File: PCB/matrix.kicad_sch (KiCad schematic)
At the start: 204 parts

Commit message: LED Diode Placement finished
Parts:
- renumbered D66 to D65, D67 to D66, D68 to D67, D69 to D68, D70 to D69, D71 to D70, D72 to D71, D73 to D72, D74 to D73, D75 to D74, D76 to D75, D77 to D76, D78 to D77, D79 to D78, D80 to D79, D81 to D80, D82 to D81, D83 to D82, D65 to D83, D87 to D84, D88 to D85, D89 to D86, D90 to D87, D91 to D88, D92 to D89, D93 to D90, D94 to D91, D95 to D92, D96 to D93, D97 to D94, D98 to D95, D84 to D96, D85 to D97, D86 to D98, MX66 to MX65, MX67 to MX66, MX68 to MX67, MX69 to MX68, MX70 to MX69, MX71 to MX70, MX72 to MX71, MX73 to MX72, MX74 to MX73, MX75 to MX74, MX76 to MX75, MX77 to MX76, MX78 to MX77, MX79 to MX78, MX80 to MX79, MX81 to MX80, MX82 to MX81, MX83 to MX82, MX65 to MX83, MX87 to MX84, MX88 to MX85, MX89 to MX86, MX90 to MX87, MX91 to MX88, MX92 to MX89, MX93 to MX90, MX94 to MX91, MX95 to MX92, MX96 to MX93, MX97 to MX94, MX98 to MX95, MX84 to MX96, MX85 to MX97, MX86 to MX98

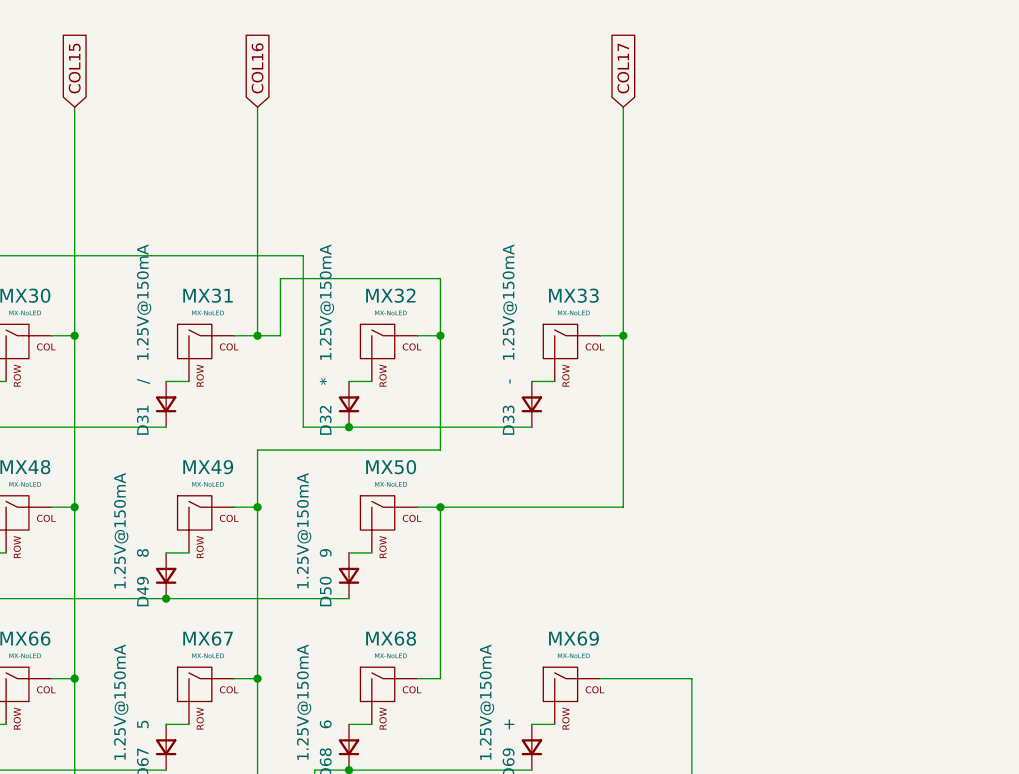
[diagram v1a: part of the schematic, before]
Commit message: LED +5 Wired, COL and ROW Buses nearly finished
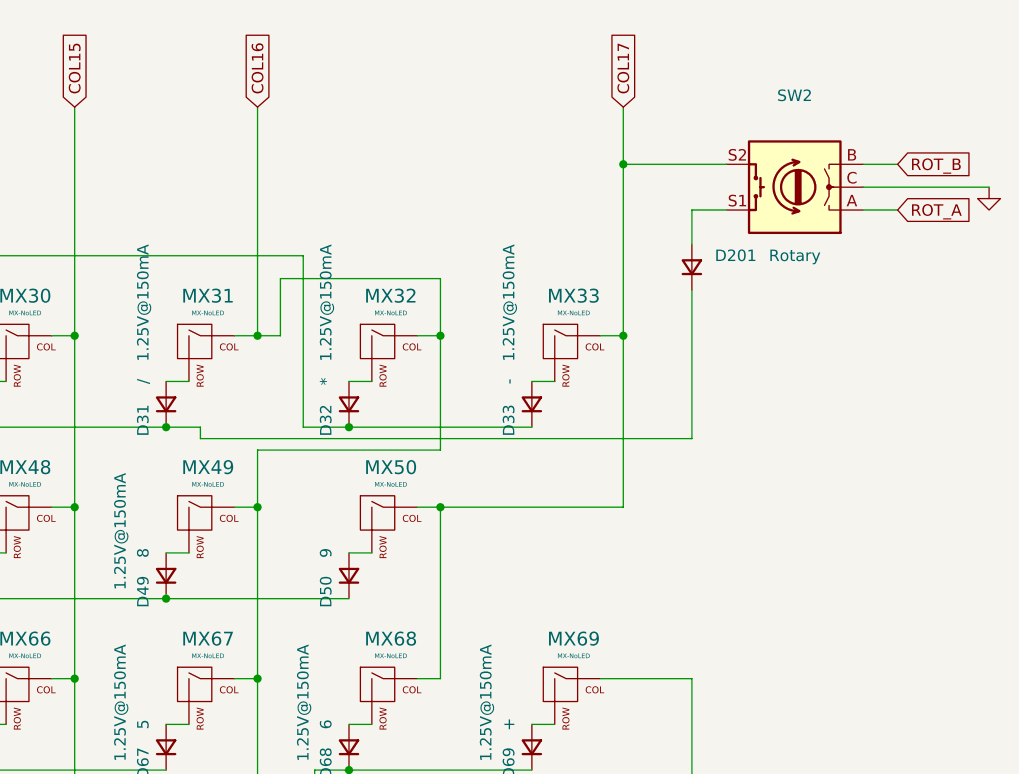
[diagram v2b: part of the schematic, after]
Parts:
- added D201: (no value), symbol led:D_Small
- added SW2: (no value), symbol Device:RotaryEncoder_Switch
- D50: value 1.25V@150mA -> (none); footprint led:D_SOD-123 -> (none)
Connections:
- net COL17: now also SW2.S2
- net ROW1: now also D201.1 (K)
- new net: D201.2 (A), SW2.S1
- new net GND: SW2.C
- new net ROT_A: SW2.A
- new net ROT_B: SW2.B
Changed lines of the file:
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@@
   (junction (at 322.58 158.75) (diameter 0) (color 0 0 0 0)
   )
+  (junction (at 459.74 168.91) (diameter 0) (color 0 0 0 0)
+  )
   (junction (at 322.58 196.85) (diameter 0) (color 0 0 0 0)
   )
@@
   (junction (at 416.56 215.9) (diameter 0) (color 0 0 0 0)
   )
+  (junction (at 510.54 139.7) (diameter 0) (color 0 0 0 0)
+  )
   (junction (at 302.26 158.75) (diameter 0) (color 0 0 0 0)
   )
@@
     (stroke (width 0) (type default) (color 0 0 0 0))
   )
+  (wire (pts (xy 510.54 139.7) (xy 521.97 139.7))
+    (stroke (width 0) (type default) (color 0 0 0 0))
+  )
   (wire (pts (xy 170.18 182.88) (xy 172.72 182.88))
     (stroke (width 0) (type default) (color 0 0 0 0))
@@
     (stroke (width 0) (type default) (color 0 0 0 0))
   )
+  (wire (pts (xy 537.21 144.78) (xy 541.02 144.78))
+    (stroke (width 0) (type default) (color 0 0 0 0))
+  )
   (wire (pts (xy 312.42 144.78) (xy 314.96 144.78))
     (stroke (width 0) (type default) (color 0 0 0 0))
@@
     (stroke (width 0) (type default) (color 0 0 0 0))
   )
+  (wire (pts (xy 537.21 142.24) (xy 551.18 142.24))
+    (stroke (width 0) (type default) (color 0 0 0 0))
+  )
   (wire (pts (xy 439.42 163.83) (xy 441.96 163.83))
     (stroke (width 0) (type default) (color 0 0 0 0))
@@
     (stroke (width 0) (type default) (color 0 0 0 0))
   )
+  (wire (pts (xy 537.21 139.7) (xy 541.02 139.7))
+    (stroke (width 0) (type default) (color 0 0 0 0))
+  )
   (wire (pts (xy 469.9 234.95) (xy 467.36 234.95))
     (stroke (width 0) (type default) (color 0 0 0 0))
@@
     (stroke (width 0) (type default) (color 0 0 0 0))
   )
+  (wire (pts (xy 510.54 139.7) (xy 510.54 133.35))
+    (stroke (width 0) (type default) (color 0 0 0 0))
+  )
   (wire (pts (xy 302.26 158.75) (xy 299.72 158.75))
     (stroke (width 0) (type default) (color 0 0 0 0))
@@
     (stroke (width 0) (type default) (color 0 0 0 0))
   )
+  (wire (pts (xy 518.16 153.67) (xy 518.16 170.18))
+    (stroke (width 0) (type default) (color 0 0 0 0))
+  )
   (wire (pts (xy 271.78 168.91) (xy 292.1 168.91))
     (stroke (width 0) (type default) (color 0 0 0 0))
@@
     (stroke (width 0) (type default) (color 0 0 0 0))
   )
+  (wire (pts (xy 463.55 170.18) (xy 518.16 170.18))
+    (stroke (width 0) (type default) (color 0 0 0 0))
+  )
   (wire (pts (xy 231.14 220.98) (xy 233.68 220.98))
     (stroke (width 0) (type default) (color 0 0 0 0))
@@
     (stroke (width 0) (type default) (color 0 0 0 0))
   )
+  (wire (pts (xy 463.55 168.91) (xy 463.55 170.18))
+    (stroke (width 0) (type default) (color 0 0 0 0))
+  )
   (wire (pts (xy 220.98 196.85) (xy 220.98 215.9))
     (stroke (width 0) (type default) (color 0 0 0 0))
@@
     (stroke (width 0) (type default) (color 0 0 0 0))
   )
+  (wire (pts (xy 459.74 168.91) (xy 463.55 168.91))
+    (stroke (width 0) (type default) (color 0 0 0 0))
+  )
   (wire (pts (xy 406.4 187.96) (xy 439.42 187.96))
     (stroke (width 0) (type default) (color 0 0 0 0))
@@
     (stroke (width 0) (type default) (color 0 0 0 0))
   )
-  (wire (pts (xy 510.54 158.75) (xy 510.54 133.35))
+  (wire (pts (xy 510.54 158.75) (xy 510.54 139.7))
     (stroke (width 0) (type default) (color 0 0 0 0))
   )
@@
     (stroke (width 0) (type default) (color 0 0 0 0))
   )
+  (wire (pts (xy 518.16 144.78) (xy 518.16 148.59))
+    (stroke (width 0) (type default) (color 0 0 0 0))
+  )
+  (wire (pts (xy 521.97 144.78) (xy 518.16 144.78))
+    (stroke (width 0) (type default) (color 0 0 0 0))
+  )
   (wire (pts (xy 116.84 196.85) (xy 119.38 196.85))
     (stroke (width 0) (type default) (color 0 0 0 0))
@@
     )
   )
+  (global_label "ROT_A" (shape input) (at 541.02 144.78 0) (fields_autoplaced)
+    (effects (font (size 1.27 1.27)) (justify left))
+    (property "Intersheet References" "${INTERSHEET_REFS}" (id 0) (at 548.9685 144.7006 0)
+      (effects (font (size 1.27 1.27)) (justify left) hide)
+    )
+  )
   (global_label "COL12" (shape input) (at 342.9 133.35 90) (fields_autoplaced)
     (effects (font (size 1.27 1.27)) (justify left))
@@
     )
   )
+  (global_label "ROT_B" (shape input) (at 541.02 139.7 0) (fields_autoplaced)
+    (effects (font (size 1.27 1.27)) (justify left))
+    (property "Intersheet References" "${INTERSHEET_REFS}" (id 0) (at 549.1499 139.6206 0)
+      (effects (font (size 1.27 1.27)) (justify left) hide)
+    )
+  )
   (global_label "COL1" (shape input) (at 119.38 133.35 90) (fields_autoplaced)
     (effects (font (size 1.27 1.27)) (justify left))
@@
       (effects (font (size 1.27 1.27)) (justify right))
     )
-    (property "Value" "1.25V@150mA" (id 1) (at 474.98 173.99 0)
+    (property "Value" "" (id 1) (at 474.98 173.99 0)
       (effects (font (size 1.27 1.27)) (justify right))
     )
-    (property "Footprint" "led:D_SOD-123" (id 2) (at 480.06 185.42 90)
+    (property "Footprint" "" (id 2) (at 480.06 185.42 90)
       (effects (font (size 1.27 1.27)) hide)
     )
@@
     (pin "2")
   )
+  (symbol (lib_id "power:GND") (at 551.18 142.24 0) (unit 1)
+    (in_bom yes) (on_board yes) (fields_autoplaced)
+    (property "Reference" "#PWR0216" (id 0) (at 551.18 148.59 0)
+      (effects (font (size 1.27 1.27)) hide)
+    )
+    (property "Value" "" (id 1) (at 551.18 147.32 0))
+    (property "Footprint" "" (id 2) (at 551.18 142.24 0)
+      (effects (font (size 1.27 1.27)) hide)
+    )
+    (property "Datasheet" "" (id 3) (at 551.18 142.24 0)
+      (effects (font (size 1.27 1.27)) hide)
+    )
+    (pin "1")
+  )
   (symbol (lib_id "Device:D_Small") (at 170.18 166.37 90) (unit 1)
     (in_bom yes) (on_board yes)
@@
     (pin "2")
   )
+  (symbol (lib_id "Device:RotaryEncoder_Switch") (at 529.59 142.24 180) (unit 1)
+    (in_bom yes) (on_board yes) (fields_autoplaced)
+    (property "Reference" "SW2" (id 0) (at 529.59 132.08 0))
+    (property "Value" "" (id 1) (at 529.59 134.62 0))
+    (property "Footprint" "" (id 2) (at 533.4 146.304 0)
+      (effects (font (size 1.27 1.27)) hide)
+    )
+    (property "Datasheet" "~" (id 3) (at 529.59 148.844 0)
+      (effects (font (size 1.27 1.27)) hide)
+    )
+    (pin "A")
+    (pin "B")
+    (pin "C")
+    (pin "S1")
+    (pin "S2")
+  )
   (symbol (lib_id "pcb-rescue:MX-NoLED-MX_Alps_Hybrid") (at 153.67 160.02 0) (unit 1)
     (in_bom yes) (on_board yes)
@@
     (pin "1")
     (pin "2")
+  )
+  (symbol (lib_id "led:D_Small") (at 518.16 151.13 90) (unit 1)
+    (in_bom yes) (on_board yes)
+    (property "Reference" "D201" (id 0) (at 520.7 149.8599 90)
+      (effects (font (size 1.27 1.27)) (justify right))
+    )
+    (property "Value" "" (id 1) (at 520.7 152.3999 90)
+      (effects (font (size 1.27 1.27)) (justify right))
+    )
+    (property "Footprint" "" (id 2) (at 518.16 140.97 90)
+      (effects (font (size 1.27 1.27)) hide)
+    )
+    (property "Datasheet" "~" (id 3) (at 518.16 151.13 90)
+      (effects (font (size 1.27 1.27)) hide)
+    )
+    (property "Name" "Rotary" (id 4) (at 529.59 149.86 90))
+    (pin "1")
+    (pin "2")

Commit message: Fixed all Errors
Only 1009 Warnings remain :D
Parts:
- removed MX101: MX-NoLED, kailh-switches-hotswap:Kailh-Hotswap-6.25U, symbol pcb-rescue:MX-NoLED-MX_Alps_Hybrid
- removed MX102: MX-NoLED, kailh-switches-hotswap:Kailh-Hotswap-7U, symbol pcb-rescue:MX-NoLED-MX_Alps_Hybrid
- removed MX103: MX-NoLED, kailh-switches-hotswap:Kailh-Hotswap-1U, symbol pcb-rescue:MX-NoLED-MX_Alps_Hybrid
- removed MX104: MX-NoLED, kailh-switches-hotswap:Kailh-Hotswap-1.25U, symbol pcb-rescue:MX-NoLED-MX_Alps_Hybrid
- D201, D50: value (none) -> 1.25V@150mA; footprint (none) -> led:D_SOD-123
- MX1, MX10, MX100, MX11, MX12, MX13, MX14, MX15, MX16, MX17, MX18, MX19, MX2, MX20, MX21, MX22, MX23, MX24, MX25, MX26, MX27, MX29, MX3, MX30, MX31, MX32, MX33, MX35, MX36, MX37, MX38, MX39, MX4, MX40, MX41, MX42, MX43, MX44, MX45, MX46, MX47, MX48, MX49, MX5, MX50, MX52, MX53, MX54, MX55, MX56, MX57, MX58, MX59, MX6, MX60, MX61, MX62, MX63, MX65, MX66, MX67, MX68, MX7, MX71, MX72, MX73, MX74, MX75, MX76, MX77, MX78, MX79, MX8, MX80, MX81, MX83, MX84, MX85, MX86, MX87, MX9, MX90, MX94, MX95, MX96, MX97, MX98: footprint kailh-switches-hotswap:Kailh-Hotswap-1U -> (none)
- MX28, MX99: footprint kailh-switches-hotswap:Kailh-Hotswap-2U -> (none)
- MX34, MX89: footprint kailh-switches-hotswap:Kailh-Hotswap-1.5U -> (none)
- MX51, MX82: footprint kailh-switches-hotswap:Kailh-Hotswap-1.75U -> (none)
- MX64: footprint kailh-switches-hotswap:Kailh-Hotswap-EnterISO -> (none)
- MX69, MX88: footprint kailh-switches-hotswap:Kailh-Hotswap-2U-Vertical -> (none)
- MX70, MX91, MX93: footprint kailh-switches-hotswap:Kailh-Hotswap-1.25U -> (none)
- MX92: footprint kailh-switches-hotswap:Kailh-Hotswap-6U -> (none)
- SW2: value (none) -> RotaryEncoder_Switch; footprint (none) -> led:RotaryEncoder_EC11E-Switch

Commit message: 3D Models
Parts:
- D1, D10, D100, D11, D12, D13, D14, D15, D16, D17, D18, D19, D2, D20, D201, D21, D22, D23, D24, D25, D26, D27, D28, D29, D3, D30, D31, D32, D33, D34, D35, D36, D37, D38, D39, D4, D40, D41, D42, D43, D44, D45, D46, D47, D48, D49, D5, D50, D51, D52, D53, D54, D55, D56, D57, D58, D59, D6, D60, D61, D62, D63, D64, D65, D66, D67, D68, D69, D7, D70, D71, D72, D73, D74, D75, D76, D77, D78, D79, D8, D80, D81, D82, D83, D84, D85, D86, D87, D88, D89, D9, D90, D91, D92, D93, D94, D95, D96, D97, D98, D99: footprint led:D_SOD-123 -> (none)

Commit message: New Connector
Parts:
- D1, D10, D100, D11, D12, D13, D14, D15, D16, D17, D18, D19, D2, D20, D201, D21, D22, D23, D24, D25, D26, D27, D28, D29, D3, D30, D31, D32, D33, D34, D35, D36, D37, D38, D39, D4, D40, D41, D42, D43, D44, D45, D46, D47, D48, D49, D5, D50, D51, D52, D53, D54, D55, D56, D57, D58, D59, D6, D60, D61, D62, D63, D64, D65, D66, D67, D68, D69, D7, D70, D71, D72, D73, D74, D75, D76, D77, D78, D79, D8, D80, D81, D82, D83, D84, D85, D86, D87, D88, D89, D9, D90, D91, D92, D93, D94, D95, D96, D97, D98, D99: footprint (none) -> led:D_SOD-123
- MX1, MX10, MX100, MX11, MX12, MX13, MX14, MX15, MX16, MX17, MX18, MX19, MX2, MX20, MX21, MX22, MX23, MX24, MX25, MX26, MX27, MX29, MX3, MX30, MX31, MX32, MX33, MX35, MX36, MX37, MX38, MX39, MX4, MX40, MX41, MX42, MX43, MX44, MX45, MX46, MX47, MX48, MX49, MX5, MX50, MX52, MX53, MX54, MX55, MX56, MX57, MX58, MX59, MX6, MX60, MX61, MX62, MX63, MX65, MX66, MX67, MX68, MX7, MX71, MX72, MX73, MX74, MX75, MX76, MX77, MX78, MX79, MX8, MX80, MX81, MX83, MX84, MX85, MX86, MX87, MX9, MX90, MX95, MX96, MX97, MX98: footprint (none) -> kailh-switches-hotswap:Kailh-Hotswap-1U
- MX28, MX99: footprint (none) -> kailh-switches-hotswap:Kailh-Hotswap-2U
- MX34, MX89: footprint (none) -> kailh-switches-hotswap:Kailh-Hotswap-1.5U
- MX51, MX82: footprint (none) -> kailh-switches-hotswap:Kailh-Hotswap-1.75U
- MX64: footprint (none) -> kailh-switches-hotswap:Kailh-Hotswap-EnterISO
- MX69, MX88: footprint (none) -> kailh-switches-hotswap:Kailh-Hotswap-2U-Vertical
- MX70, MX91: footprint (none) -> kailh-switches-hotswap:Kailh-Hotswap-1.25U
- MX92: footprint (none) -> kailh-switches-hotswap:Kailh-Hotswap-6U-6.25U-7U
- MX93, MX94: footprint (none) -> kailh-switches-hotswap:Kailh-Hotswap-1U-1.25U

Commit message: Now only 2 alternative bottom rows
6.25U (Three 1U Keys to the right) and 7U (One 1.25U Key and one 1U Key to the right) Space Supported

Also new rounded PCB
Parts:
- MX92: footprint kailh-switches-hotswap:Kailh-Hotswap-6U-6.25U-7U -> (none)
- MX93: footprint kailh-switches-hotswap:Kailh-Hotswap-1U-1.25U -> (none)
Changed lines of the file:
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@@
       (effects (font (size 0.508 0.508)))
     )
-    (property "Footprint" "kailh-switches-hotswap:Kailh-Hotswap-6U-6.25U-7U" (id 2) (at 198.755 236.855 0)
+    (property "Footprint" "" (id 2) (at 198.755 236.855 0)
       (effects (font (size 1.524 1.524)) hide)
     )
@@
       (effects (font (size 0.508 0.508)))
     )
-    (property "Footprint" "kailh-switches-hotswap:Kailh-Hotswap-1U-1.25U" (id 2) (at 258.445 236.855 0)
-      (effects (font (size 1.524 1.524)) hide)
-    )
+    (property "Footprint" "" (id 2) (at 258.445 236.855 0)
+      (effects (font (size 1.524 1.524)) hide)
+    )

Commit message: datalines and mosfet
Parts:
- MX92: footprint (none) -> kailh-switches-hotswap:Kailh-Hotswap-6.25U-7U
- MX93: footprint (none) -> kailh-switches-hotswap:Kailh-Hotswap-1U
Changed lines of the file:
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@@
       (effects (font (size 0.508 0.508)))
     )
-    (property "Footprint" "" (id 2) (at 198.755 236.855 0)
+    (property "Footprint" "kailh-switches-hotswap:Kailh-Hotswap-6.25U-7U" (id 2) (at 198.755 236.855 0)
       (effects (font (size 1.524 1.524)) hide)
     )
@@
       (effects (font (size 0.508 0.508)))
     )
-    (property "Footprint" "" (id 2) (at 258.445 236.855 0)
-      (effects (font (size 1.524 1.524)) hide)
-    )
+    (property "Footprint" "kailh-switches-hotswap:Kailh-Hotswap-1U" (id 2) (at 258.445 236.855 0)
+      (effects (font (size 1.524 1.524)) hide)
+    )

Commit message: changes:\n\n -change zones\n -add mounting holes\n -change via size
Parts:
- added H1, H2, H3, H4, H5, H6, H7, H8, H9: MountingHole, symbol Mechanical:MountingHole
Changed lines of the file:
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@@
     (pin "2")
+  )
+  (symbol (lib_id "Mechanical:MountingHole") (at 504.19 240.665 0) (unit 1)
+    (in_bom yes) (on_board yes) (fields_autoplaced)
+    (property "Reference" "H9" (id 0) (at 506.73 239.3949 0)
+      (effects (font (size 1.27 1.27)) (justify left))
+    )
+    (property "Value" "MountingHole" (id 1) (at 506.73 241.9349 0)
+      (effects (font (size 1.27 1.27)) (justify left))
+    )
+    (property "Footprint" "" (id 2) (at 504.19 240.665 0)
+      (effects (font (size 1.27 1.27)) hide)
+    )
+    (property "Datasheet" "~" (id 3) (at 504.19 240.665 0)
+      (effects (font (size 1.27 1.27)) hide)
+    )
   )
   (symbol (lib_id "Device:D_Small") (at 439.42 166.37 90) (unit 1)
@@
     (pin "2")
   )
+  (symbol (lib_id "Mechanical:MountingHole") (at 107.95 229.235 0) (unit 1)
+    (in_bom yes) (on_board yes) (fields_autoplaced)
+    (property "Reference" "H1" (id 0) (at 110.49 227.9649 0)
+      (effects (font (size 1.27 1.27)) (justify left))
+    )
+    (property "Value" "MountingHole" (id 1) (at 110.49 230.5049 0)
+      (effects (font (size 1.27 1.27)) (justify left))
+    )
+    (property "Footprint" "" (id 2) (at 107.95 229.235 0)
+      (effects (font (size 1.27 1.27)) hide)
+    )
+    (property "Datasheet" "~" (id 3) (at 107.95 229.235 0)
+      (effects (font (size 1.27 1.27)) hide)
+    )
+  )
   (symbol (lib_id "pcb-rescue:MX-NoLED-MX_Alps_Hybrid") (at 133.35 160.02 0) (unit 1)
     (in_bom yes) (on_board yes)
@@
     (pin "2")
   )
+  (symbol (lib_id "Mechanical:MountingHole") (at 306.705 187.96 0) (unit 1)
+    (in_bom yes) (on_board yes) (fields_autoplaced)
+    (property "Reference" "H5" (id 0) (at 309.245 186.6899 0)
+      (effects (font (size 1.27 1.27)) (justify left))
+    )
+    (property "Value" "MountingHole" (id 1) (at 309.245 189.2299 0)
+      (effects (font (size 1.27 1.27)) (justify left))
+    )
+    (property "Footprint" "" (id 2) (at 306.705 187.96 0)
+      (effects (font (size 1.27 1.27)) hide)
+    )
+    (property "Datasheet" "~" (id 3) (at 306.705 187.96 0)
+      (effects (font (size 1.27 1.27)) hide)
+    )
+  )
   (symbol (lib_id "Device:D_Small") (at 379.73 248.92 90) (unit 1)
     (in_bom yes) (on_board yes)
@@
     (pin "1")
     (pin "2")
+  )
+  (symbol (lib_id "Mechanical:MountingHole") (at 221.615 149.86 0) (unit 1)
+    (in_bom yes) (on_board yes) (fields_autoplaced)
+    (property "Reference" "H4" (id 0) (at 224.155 148.5899 0)
+      (effects (font (size 1.27 1.27)) (justify left))
+    )
+    (property "Value" "MountingHole" (id 1) (at 224.155 151.1299 0)
+      (effects (font (size 1.27 1.27)) (justify left))
+    )
+    (property "Footprint" "" (id 2) (at 221.615 149.86 0)
+      (effects (font (size 1.27 1.27)) hide)
+    )
+    (property "Datasheet" "~" (id 3) (at 221.615 149.86 0)
+      (effects (font (size 1.27 1.27)) hide)
+    )
   )
   (symbol (lib_id "Device:D_Small") (at 190.5 204.47 90) (unit 1)
@@
     (pin "2")
   )
+  (symbol (lib_id "Mechanical:MountingHole") (at 401.955 224.79 0) (unit 1)
+    (in_bom yes) (on_board yes) (fields_autoplaced)
+    (property "Reference" "H7" (id 0) (at 404.495 223.5199 0)
+      (effects (font (size 1.27 1.27)) (justify left))
+    )
+    (property "Value" "MountingHole" (id 1) (at 404.495 226.0599 0)
+      (effects (font (size 1.27 1.27)) (justify left))
+    )
+    (property "Footprint" "" (id 2) (at 401.955 224.79 0)
+      (effects (font (size 1.27 1.27)) hide)
+    )
+    (property "Datasheet" "~" (id 3) (at 401.955 224.79 0)
+      (effects (font (size 1.27 1.27)) hide)
+    )
+  )
   (symbol (lib_id "pcb-rescue:MX-NoLED-MX_Alps_Hybrid") (at 463.55 236.22 0) (unit 1)
     (in_bom yes) (on_board yes)
@@
     (pin "2")
   )
+  (symbol (lib_id "Mechanical:MountingHole") (at 220.98 229.235 0) (unit 1)
+    (in_bom yes) (on_board yes) (fields_autoplaced)
+    (property "Reference" "H3" (id 0) (at 223.52 227.9649 0)
+      (effects (font (size 1.27 1.27)) (justify left))
+    )
+    (property "Value" "MountingHole" (id 1) (at 223.52 230.5049 0)
+      (effects (font (size 1.27 1.27)) (justify left))
+    )
+    (property "Footprint" "" (id 2) (at 220.98 229.235 0)
+      (effects (font (size 1.27 1.27)) hide)
+    )
+    (property "Datasheet" "~" (id 3) (at 220.98 229.235 0)
+      (effects (font (size 1.27 1.27)) hide)
+    )
+  )
+  (symbol (lib_id "Mechanical:MountingHole") (at 391.16 149.225 0) (unit 1)
+    (in_bom yes) (on_board yes) (fields_autoplaced)
+    (property "Reference" "H6" (id 0) (at 393.7 147.9549 0)
+      (effects (font (size 1.27 1.27)) (justify left))
+    )
+    (property "Value" "MountingHole" (id 1) (at 393.7 150.4949 0)
+      (effects (font (size 1.27 1.27)) (justify left))
+    )
+    (property "Footprint" "" (id 2) (at 391.16 149.225 0)
+      (effects (font (size 1.27 1.27)) hide)
+    )
+    (property "Datasheet" "~" (id 3) (at 391.16 149.225 0)
+      (effects (font (size 1.27 1.27)) hide)
+    )
+  )
   (symbol (lib_id "Device:D_Small") (at 312.42 166.37 90) (unit 1)
     (in_bom yes) (on_board yes)
@@
     (pin "2")
   )
+  (symbol (lib_id "Mechanical:MountingHole") (at 109.855 149.225 0) (unit 1)
+    (in_bom yes) (on_board yes) (fields_autoplaced)
+    (property "Reference" "H2" (id 0) (at 112.395 147.9549 0)
+      (effects (font (size 1.27 1.27)) (justify left))
+    )
+    (property "Value" "MountingHole" (id 1) (at 112.395 150.4949 0)
+      (effects (font (size 1.27 1.27)) (justify left))
+    )
+    (property "Footprint" "" (id 2) (at 109.855 149.225 0)
+      (effects (font (size 1.27 1.27)) hide)
+    )
+    (property "Datasheet" "~" (id 3) (at 109.855 149.225 0)
+      (effects (font (size 1.27 1.27)) hide)
+    )
+  )
+  (symbol (lib_id "Mechanical:MountingHole") (at 498.475 146.05 0) (unit 1)
+    (in_bom yes) (on_board yes) (fields_autoplaced)
+    (property "Reference" "H8" (id 0) (at 501.015 144.7799 0)
+      (effects (font (size 1.27 1.27)) (justify left))
+    )
+    (property "Value" "MountingHole" (id 1) (at 501.015 147.3199 0)
+      (effects (font (size 1.27 1.27)) (justify left))
+    )
+    (property "Footprint" "" (id 2) (at 498.475 146.05 0)
+      (effects (font (size 1.27 1.27)) hide)
+    )
+    (property "Datasheet" "~" (id 3) (at 498.475 146.05 0)
+      (effects (font (size 1.27 1.27)) hide)
+    )
+  )
   (symbol (lib_id "Device:D_Small") (at 231.14 185.42 90) (unit 1)
